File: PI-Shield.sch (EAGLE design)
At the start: 80 parts, among them IC1 PCF8574T, J10 T2I, J11 T2I, J12 T2I, J13 DF13-4P-1.25DSA, J14 DF13-4P-1.25DSA, J15 DF13-4P-1.25DSA, Q1 220mA/50V/3.5Ω, Q2 220mA/50V/3.5Ω, Q3 220mA/50V/3.5Ω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

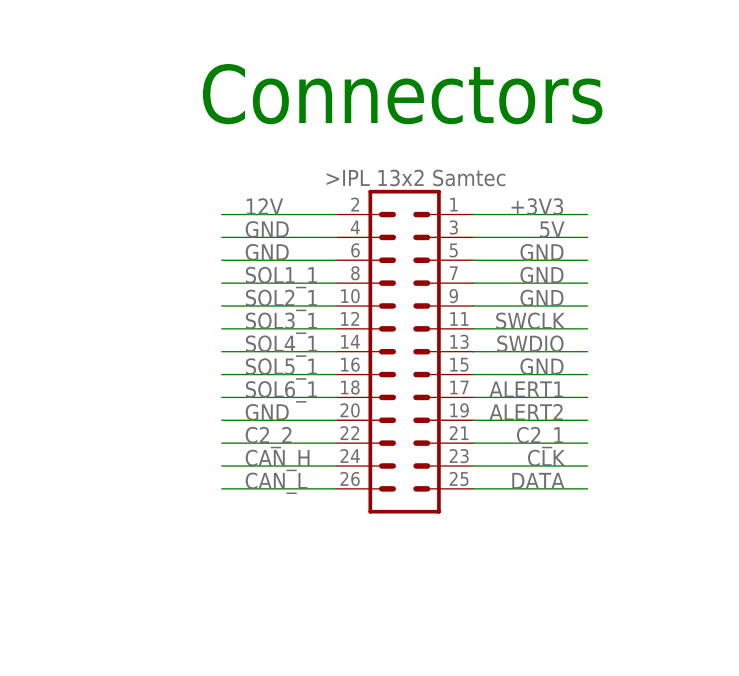
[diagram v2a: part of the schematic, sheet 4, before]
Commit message: Board Update
Changes: [Reduced backplane connector from 26->12 positions, added board outline matching last year's, placement of components]
To Do: [Routing, which should be done within next 24 hrs :P]
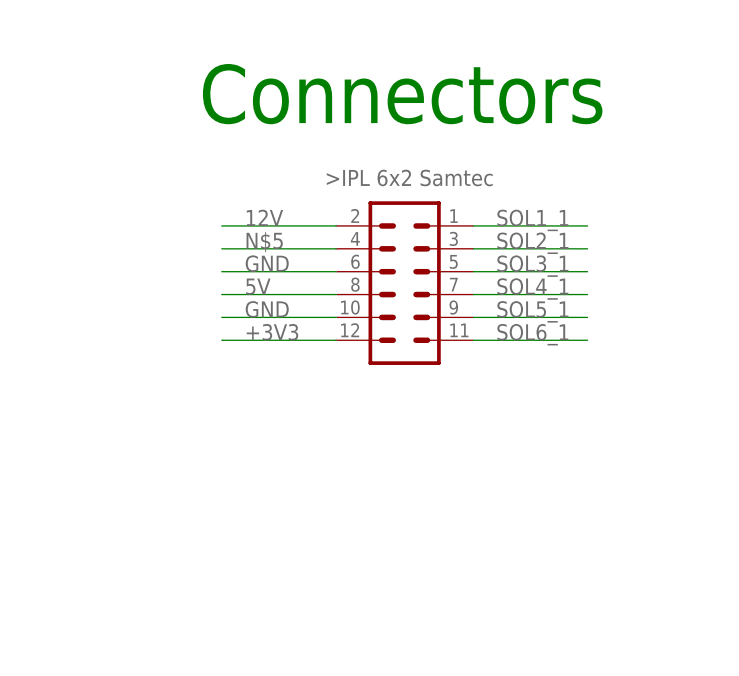
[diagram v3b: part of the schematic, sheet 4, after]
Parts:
- U$3: value IPL_13X2 -> 6X_CONN; device PI-SHIELD, Solenoid-Backplane:IPL_13X2 -> PI-SHIELD, Solenoid-Backplane:6X_CONN
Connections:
- removed net ALERT1: U$3.16
- removed net ALERT2: U$3.18
- removed net C2_1: U$3.20
- removed net C2_2: U$3.19
- removed net DATA: U$3.24
- removed net SWCLK: U$3.10
- removed net SWDIO: U$3.12
- new net N$5: U$3.15
- net +3V3: now also U$3.23; no longer U$3.26
- net 12V: now also U$3.13; no longer U$3.25
- net 5V: now also U$3.19; no longer U$3.2
- net CAN_H: no longer U$3.21
- net CAN_L: no longer U$3.23
- net CLK: no longer U$3.22
- net GND: now also U$3.21; no longer U$3.1, U$3.14, U$3.3, U$3.4, U$3.6, U$3.8
- net SOL1_1: now also U$3.14; no longer U$3.5
- net SOL2_1: now also U$3.16; no longer U$3.7
- net SOL3_1: now also U$3.18; no longer U$3.9
- net SOL4_1: now also U$3.20; no longer U$3.11
- net SOL5_1: now also U$3.22; no longer U$3.13
- net SOL6_1: now also U$3.24; no longer U$3.15
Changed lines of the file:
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@@
 <part name="SUPPLY1" library="supply2" library_urn="urn:adsk.eagle:library:372" deviceset="GND" device=""/>
 <part name="C15" library="SparkFun-Capacitors" library_urn="urn:adsk.eagle:library:510" deviceset="47UF-POLAR" device="-PANASONIC_D-35V-20%" package3d_urn="urn:adsk.eagle:package:37420/1" value="47uF"/>
-<part name="U$3" library="PI-SHIELD, Solenoid-Backplane" deviceset="IPL_13X2" device=""/>
+<part name="U$3" library="PI-SHIELD, Solenoid-Backplane" deviceset="6X_CONN" device=""/>
 </parts>
 <sheets>
@@
 <attribute name="VALUE" x="69.596" y="44.069" size="1.778" layer="96" font="vector"/>
 </instance>
-<instance part="U$3" gate="G$1" x="203.2" y="124.46" smashed="yes"/>
+<instance part="U$3" gate="G$1" x="203.2" y="132.08" smashed="yes"/>
 </instances>
 <busses>
@@
 </segment>
 <segment>
-<pinref part="U$3" gate="G$1" pin="4"/>
-<wire x1="210.82" y1="134.62" x2="223.52" y2="134.62" width="0.1524" layer="91"/>
-<label x="220.98" y="134.62" size="1.778" layer="95" align="bottom-right"/>
-</segment>
-<segment>
-<pinref part="U$3" gate="G$1" pin="6"/>
-<wire x1="210.82" y1="132.08" x2="223.52" y2="132.08" width="0.1524" layer="91"/>
-<label x="220.98" y="132.08" size="1.778" layer="95" align="bottom-right"/>
-</segment>
-<segment>
-<pinref part="U$3" gate="G$1" pin="8"/>
-<wire x1="210.82" y1="129.54" x2="223.52" y2="129.54" width="0.1524" layer="91"/>
-<label x="220.98" y="129.54" size="1.778" layer="95" align="bottom-right"/>
-</segment>
-<segment>
-<pinref part="U$3" gate="G$1" pin="1"/>
-<wire x1="195.58" y1="137.16" x2="182.88" y2="137.16" width="0.1524" layer="91"/>
-<label x="185.42" y="137.16" size="1.778" layer="95"/>
-</segment>
-<segment>
-<pinref part="U$3" gate="G$1" pin="3"/>
-<wire x1="195.58" y1="134.62" x2="182.88" y2="134.62" width="0.1524" layer="91"/>
-<label x="185.42" y="134.62" size="1.778" layer="95"/>
-</segment>
-<segment>
+<wire x1="195.58" y1="133.35" x2="182.88" y2="133.35" width="0.1524" layer="91"/>
+<label x="185.42" y="133.35" size="1.778" layer="95"/>
 <pinref part="U$3" gate="G$1" pin="17"/>
-<wire x1="195.58" y1="116.84" x2="182.88" y2="116.84" width="0.1524" layer="91"/>
-<label x="185.42" y="116.84" size="1.778" layer="95"/>
-</segment>
-<segment>
-<pinref part="U$3" gate="G$1" pin="14"/>
-<wire x1="210.82" y1="121.92" x2="223.52" y2="121.92" width="0.1524" layer="91"/>
-<label x="220.98" y="121.92" size="1.778" layer="95" align="bottom-right"/>
+</segment>
+<segment>
+<wire x1="195.58" y1="128.27" x2="182.88" y2="128.27" width="0.1524" layer="91"/>
+<label x="185.42" y="128.27" size="1.778" layer="95"/>
+<pinref part="U$3" gate="G$1" pin="21"/>
 </segment>
 </net>
@@
 </segment>
 <segment>
-<pinref part="U$3" gate="G$1" pin="25"/>
-<wire x1="195.58" y1="139.7" x2="182.88" y2="139.7" width="0.1524" layer="91"/>
-<label x="185.42" y="139.7" size="1.778" layer="95"/>
+<wire x1="195.58" y1="138.43" x2="182.88" y2="138.43" width="0.1524" layer="91"/>
+<label x="185.42" y="138.43" size="1.778" layer="95"/>
+<pinref part="U$3" gate="G$1" pin="13"/>
 </segment>
 </net>
@@
 </segment>
 <segment>
-<pinref part="U$3" gate="G$1" pin="5"/>
-<wire x1="195.58" y1="132.08" x2="182.88" y2="132.08" width="0.1524" layer="91"/>
-<label x="185.42" y="132.08" size="1.778" layer="95"/>
+<wire x1="223.52" y1="138.43" x2="210.82" y2="138.43" width="0.1524" layer="91"/>
+<label x="213.36" y="138.43" size="1.778" layer="95"/>
+<pinref part="U$3" gate="G$1" pin="14"/>
 </segment>
 </net>
@@
 </segment>
 <segment>
-<pinref part="U$3" gate="G$1" pin="7"/>
-<wire x1="195.58" y1="129.54" x2="182.88" y2="129.54" width="0.1524" layer="91"/>
-<label x="185.42" y="129.54" size="1.778" layer="95"/>
+<wire x1="223.52" y1="135.89" x2="210.82" y2="135.89" width="0.1524" layer="91"/>
+<label x="213.36" y="135.89" size="1.778" layer="95"/>
+<pinref part="U$3" gate="G$1" pin="16"/>
 </segment>
 </net>
@@
 </segment>
 <segment>
-<pinref part="U$3" gate="G$1" pin="9"/>
-<wire x1="195.58" y1="127" x2="182.88" y2="127" width="0.1524" layer="91"/>
-<label x="185.42" y="127" size="1.778" layer="95"/>
+<wire x1="223.52" y1="133.35" x2="210.82" y2="133.35" width="0.1524" layer="91"/>
+<label x="213.36" y="133.35" size="1.778" layer="95"/>
+<pinref part="U$3" gate="G$1" pin="18"/>
 </segment>
 </net>
@@
 </segment>
 <segment>
-<pinref part="U$3" gate="G$1" pin="11"/>
-<wire x1="195.58" y1="124.46" x2="182.88" y2="124.46" width="0.1524" layer="91"/>
-<label x="185.42" y="124.46" size="1.778" layer="95"/>
+<wire x1="223.52" y1="130.81" x2="210.82" y2="130.81" width="0.1524" layer="91"/>
+<label x="213.36" y="130.81" size="1.778" layer="95"/>
+<pinref part="U$3" gate="G$1" pin="20"/>
 </segment>
 </net>
@@
 </segment>
 <segment>
-<pinref part="U$3" gate="G$1" pin="13"/>
-<wire x1="195.58" y1="121.92" x2="182.88" y2="121.92" width="0.1524" layer="91"/>
-<label x="185.42" y="121.92" size="1.778" layer="95"/>
+<wire x1="223.52" y1="128.27" x2="210.82" y2="128.27" width="0.1524" layer="91"/>
+<label x="213.36" y="128.27" size="1.778" layer="95"/>
+<pinref part="U$3" gate="G$1" pin="22"/>
 </segment>
 </net>
@@
 </segment>
 <segment>
-<pinref part="U$3" gate="G$1" pin="15"/>
-<wire x1="195.58" y1="119.38" x2="182.88" y2="119.38" width="0.1524" layer="91"/>
-<label x="185.42" y="119.38" size="1.778" layer="95"/>
+<wire x1="223.52" y1="125.73" x2="210.82" y2="125.73" width="0.1524" layer="91"/>
+<label x="213.36" y="125.73" size="1.778" layer="95"/>
+<pinref part="U$3" gate="G$1" pin="24"/>
 </segment>
 </net>
@@
 </segment>
 <segment>
-<pinref part="U$3" gate="G$1" pin="26"/>
-<wire x1="210.82" y1="139.7" x2="223.52" y2="139.7" width="0.1524" layer="91"/>
-<label x="220.98" y="139.7" size="1.778" layer="95" align="bottom-right"/>
-</segment>
-</net>
-<net name="SWDIO" class="0">
-<segment>
-<pinref part="U$3" gate="G$1" pin="12"/>
-<wire x1="210.82" y1="124.46" x2="223.52" y2="124.46" width="0.1524" layer="91"/>
-<label x="220.98" y="124.46" size="1.778" layer="95" align="bottom-right"/>
-</segment>
-</net>
-<net name="SWCLK" class="0">
-<segment>
-<pinref part="U$3" gate="G$1" pin="10"/>
-<wire x1="210.82" y1="127" x2="223.52" y2="127" width="0.1524" layer="91"/>
-<label x="220.98" y="127" size="1.778" layer="95" align="bottom-right"/>
-</segment>
-</net>
-<net name="C2_1" class="0">
-<segment>
-<pinref part="U$3" gate="G$1" pin="20"/>
-<wire x1="210.82" y1="114.3" x2="223.52" y2="114.3" width="0.1524" layer="91"/>
-<label x="220.98" y="114.3" size="1.778" layer="95" align="bottom-right"/>
-</segment>
-</net>
-<net name="CLK" class="0">
-<segment>
-<pinref part="U$3" gate="G$1" pin="22"/>
-<wire x1="210.82" y1="111.76" x2="223.52" y2="111.76" width="0.1524" layer="91"/>
-<label x="220.98" y="111.76" size="1.778" layer="95" align="bottom-right"/>
-</segment>
-</net>
-<net name="ALERT1" class="0">
-<segment>
-<pinref part="U$3" gate="G$1" pin="16"/>
-<wire x1="210.82" y1="119.38" x2="223.52" y2="119.38" width="0.1524" layer="91"/>
-<label x="220.98" y="119.38" size="1.778" layer="95" align="bottom-right"/>
+<wire x1="182.88" y1="125.73" x2="195.58" y2="125.73" width="0.1524" layer="91"/>
+<pinref part="U$3" gate="G$1" pin="23"/>
+<label x="185.42" y="125.73" size="1.778" layer="95"/>
 </segment>
 </net>
@@
 </segment>
 </net>
+<net name="N$5" class="0">
+<segment>
+<wire x1="195.58" y1="135.89" x2="182.88" y2="135.89" width="0.1524" layer="91"/>
+<label x="185.42" y="135.89" size="1.778" layer="95"/>
+<pinref part="U$3" gate="G$1" pin="15"/>
+</segment>
+</net>
 <net name="5V" class="2">
 <segment>
-<pinref part="U$3" gate="G$1" pin="2"/>
-<wire x1="210.82" y1="137.16" x2="223.52" y2="137.16" width="0.1524" layer="91"/>
-<label x="220.98" y="137.16" size="1.778" layer="95" align="bottom-right"/>
-</segment>
-</net>
-<net name="CAN_H" class="1">
-<segment>
-<pinref part="U$3" gate="G$1" pin="21"/>
-<wire x1="195.58" y1="111.76" x2="182.88" y2="111.76" width="0.1524" layer="91"/>
-<label x="185.42" y="111.76" size="1.778" layer="95"/>
-</segment>
-</net>
-<net name="CAN_L" class="1">
-<segment>
-<pinref part="U$3" gate="G$1" pin="23"/>
-<wire x1="195.58" y1="109.22" x2="182.88" y2="109.22" width="0.1524" layer="91"/>
-<label x="185.42" y="109.22" size="1.778" layer="95"/>
-</segment>
-</net>
-<net name="DATA" class="0">
-<segment>
-<pinref part="U$3" gate="G$1" pin="24"/>
-<wire x1="210.82" y1="109.22" x2="223.52" y2="109.22" width="0.1524" layer="91"/>
-<label x="220.98" y="109.22" size="1.778" layer="95" align="bottom-right"/>
-</segment>
-</net>
-<net name="C2_2" class="0">
-<segment>
+<wire x1="195.58" y1="130.81" x2="182.88" y2="130.81" width="0.1524" layer="91"/>
 <pinref part="U$3" gate="G$1" pin="19"/>
-<wire x1="195.58" y1="114.3" x2="182.88" y2="114.3" width="0.1524" layer="91"/>
-<label x="185.42" y="114.3" size="1.778" layer="95"/>
-</segment>
-</net>
-<net name="ALERT2" class="0">
-<segment>
-<pinref part="U$3" gate="G$1" pin="18"/>
-<wire x1="210.82" y1="116.84" x2="223.52" y2="116.84" width="0.1524" layer="91"/>
-<label x="220.98" y="116.84" size="1.778" layer="95" align="bottom-right"/>
-</segment>
-</net>
+<label x="185.42" y="130.81" size="1.778" layer="95"/>
+</segment>
+</net>

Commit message: Schematic Update
Changes: [FREAKING FORGOT TO LABEL A PIN >:((((]
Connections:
- removed net N$5: U$3.15
- net 12V: now also U$3.15
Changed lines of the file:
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@@
 <pinref part="U$3" gate="G$1" pin="13"/>
+</segment>
+<segment>
+<wire x1="195.58" y1="135.89" x2="182.88" y2="135.89" width="0.1524" layer="91"/>
+<label x="185.42" y="135.89" size="1.778" layer="95"/>
+<pinref part="U$3" gate="G$1" pin="15"/>
 </segment>
 </net>
@@
 </segment>
 </net>
-<net name="N$5" class="0">
-<segment>
-<wire x1="195.58" y1="135.89" x2="182.88" y2="135.89" width="0.1524" layer="91"/>
-<label x="185.42" y="135.89" size="1.778" layer="95"/>
-<pinref part="U$3" gate="G$1" pin="15"/>
-</segment>
-</net>

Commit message: Alumni Design Updates
Changes: [Trace Matched SCL/SDA & TX/RX, added alumni feedback]
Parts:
- removed C11, C12: 4.7uF, SparkFun-Capacitors:22NF/22,000PF-0603-50V-10%
- removed U2: AZ1117EH-3.3TRG1, AZ1117EH-3.3TRG1:AZ1117EH-3.3TRG1
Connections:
- removed net +3V3: IC1.VDD, U$3.23
- net 3V3: now also IC1.VDD, U$3.23; no longer C12.1, U2.OUT
- net 5V: no longer C11.1, U2.IN
- net GND: no longer C11.2, C12.2, U2.ADJ/GND
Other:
- note removed: "Linear Regulator"
- note removed: "Obsolete Product Needs to be replaced"
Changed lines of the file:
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@@
 <part name="R14" library="SparkFun-Resistors" library_urn="urn:adsk.eagle:library:532" deviceset="RESISTOR" device="0603" package3d_urn="urn:adsk.eagle:package:39650/1" value=" "/>
 <part name="R15" library="SparkFun-Resistors" library_urn="urn:adsk.eagle:library:532" deviceset="RESISTOR" device="0603" package3d_urn="urn:adsk.eagle:package:39650/1" value=" "/>
-<part name="U2" library="AZ1117EH-3.3TRG1" deviceset="AZ1117EH-3.3TRG1" device=""/>
-<part name="C11" library="SparkFun-Capacitors" library_urn="urn:adsk.eagle:library:510" deviceset="22NF/22,000PF" device="-0603-50V-10%" package3d_urn="urn:adsk.eagle:package:37414/1" value="4.7uF"/>
-<part name="C12" library="SparkFun-Capacitors" library_urn="urn:adsk.eagle:library:510" deviceset="22NF/22,000PF" device="-0603-50V-10%" package3d_urn="urn:adsk.eagle:package:37414/1" value="4.7uF"/>
 <part name="J2" library="SparkFun-Connectors" deviceset="CONN_04" device=""/>
 <part name="J6" library="SparkFun-Connectors" deviceset="CONN_02" device=""/>
@@
 <part name="R16" library="SparkFun-Resistors" library_urn="urn:adsk.eagle:library:532" deviceset="RESISTOR" device="0603" package3d_urn="urn:adsk.eagle:package:39650/1" value=" "/>
 <part name="GND30" library="supply1" library_urn="urn:adsk.eagle:library:371" deviceset="GND" device=""/>
-<part name="GND32" library="supply1" library_urn="urn:adsk.eagle:library:371" deviceset="GND" device=""/>
 <part name="GND33" library="supply1" library_urn="urn:adsk.eagle:library:371" deviceset="GND" device=""/>
-<part name="GND34" library="supply1" library_urn="urn:adsk.eagle:library:371" deviceset="GND" device=""/>
 <part name="GND35" library="supply1" library_urn="urn:adsk.eagle:library:371" deviceset="GND" device=""/>
 <part name="GND36" library="supply1" library_urn="urn:adsk.eagle:library:371" deviceset="GND" device=""/>
@@
 Note: 2 NMOS for each
 Open Drain Driver (SDA, SCL)</text>
-<text x="40.64" y="160.02" size="1.778" layer="91">Linear Regulator</text>
 <text x="15.24" y="73.66" size="1.778" layer="91">Do NOT solder this 0Ohm resistor
 unless current sensor is not soldered;
@@
 <text x="73.66" y="111.76" size="1.778" layer="91">Need to replace the sensor sensor with one in stock</text>
 <text x="129.54" y="162.56" size="1.778" layer="91">Should replace the ADC with a cheaper one</text>
-<text x="66.04" y="160.02" size="1.778" layer="91">Obsolete Product
-Needs to be replaced</text>
 <text x="7.62" y="43.18" size="1.778" layer="91">Power Indicator LEDs</text>
 <text x="68.58" y="43.18" size="1.778" layer="91">VOC Pin on MCR1101 determines current
@@
 <attribute name="VALUE" x="177.8" y="105.664" size="1.778" layer="96" font="vector" rot="R180" align="top-center"/>
 </instance>
-<instance part="U2" gate="G$1" x="48.26" y="147.32" smashed="yes">
-<attribute name="NAME" x="40.63058125" y="152.40628125" size="1.7802" layer="95"/>
-<attribute name="VALUE" x="40.632559375" y="139.692559375" size="1.779740625" layer="96"/>
-</instance>
-<instance part="C11" gate="G$1" x="30.48" y="142.24" smashed="yes">
-<attribute name="NAME" x="32.004" y="145.161" size="1.778" layer="95" font="vector"/>
-<attribute name="VALUE" x="32.004" y="140.081" size="1.778" layer="96" font="vector"/>
-</instance>
-<instance part="C12" gate="G$1" x="71.12" y="144.78" smashed="yes">
-<attribute name="NAME" x="72.644" y="147.701" size="1.778" layer="95" font="vector"/>
-<attribute name="VALUE" x="72.644" y="142.621" size="1.778" layer="96" font="vector"/>
-</instance>
 <instance part="J2" gate="G$1" x="33.02" y="109.22" smashed="yes">
 <attribute name="VALUE" x="27.94" y="101.854" size="1.778" layer="96" font="vector"/>
@@
 <attribute name="VALUE" x="121.92" y="119.38" size="1.778" layer="96"/>
 </instance>
-<instance part="GND32" gate="1" x="68.58" y="137.16" smashed="yes">
-<attribute name="VALUE" x="66.04" y="134.62" size="1.778" layer="96"/>
-</instance>
 <instance part="GND33" gate="1" x="175.26" y="30.48" smashed="yes">
 <attribute name="VALUE" x="172.72" y="27.94" size="1.778" layer="96"/>
-</instance>
-<instance part="GND34" gate="1" x="30.48" y="134.62" smashed="yes">
-<attribute name="VALUE" x="27.94" y="132.08" size="1.778" layer="96"/>
 </instance>
 <instance part="GND35" gate="1" x="231.14" y="43.18" smashed="yes">
@@
 <wire x1="124.46" y1="127" x2="124.46" y2="124.46" width="0.1524" layer="91"/>
 <pinref part="GND30" gate="1" pin="GND"/>
-</segment>
-<segment>
-<pinref part="C11" gate="G$1" pin="2"/>
-<wire x1="30.48" y1="139.7" x2="30.48" y2="137.16" width="0.1524" layer="91"/>
-<pinref part="GND34" gate="1" pin="GND"/>
-</segment>
-<segment>
-<pinref part="U2" gate="G$1" pin="ADJ/GND"/>
-<wire x1="58.42" y1="144.78" x2="66.04" y2="144.78" width="0.1524" layer="91"/>
-<wire x1="66.04" y1="144.78" x2="66.04" y2="139.7" width="0.1524" layer="91"/>
-<wire x1="66.04" y1="139.7" x2="68.58" y2="139.7" width="0.1524" layer="91"/>
-<pinref part="GND32" gate="1" pin="GND"/>
-<pinref part="C12" gate="G$1" pin="2"/>
-<wire x1="71.12" y1="142.24" x2="71.12" y2="139.7" width="0.1524" layer="91"/>
-<wire x1="71.12" y1="139.7" x2="68.58" y2="139.7" width="0.1524" layer="91"/>
-<junction x="68.58" y="139.7"/>
 </segment>
 <segment>
@@
 <wire x1="233.68" y1="129.54" x2="236.22" y2="129.54" width="0.1524" layer="91"/>
 <label x="236.22" y="129.54" size="1.778" layer="95"/>
-</segment>
-<segment>
-<pinref part="U2" gate="G$1" pin="IN"/>
-<wire x1="38.1" y1="149.86" x2="30.48" y2="149.86" width="0.1524" layer="91"/>
-<pinref part="C11" gate="G$1" pin="1"/>
-<wire x1="30.48" y1="149.86" x2="30.48" y2="147.32" width="0.1524" layer="91"/>
-<wire x1="30.48" y1="149.86" x2="27.94" y2="149.86" width="0.1524" layer="91"/>
-<junction x="30.48" y="149.86"/>
-<wire x1="27.94" y1="149.86" x2="27.94" y2="152.4" width="0.1524" layer="91"/>
-<label x="27.94" y="152.4" size="1.778" layer="95" rot="R180" xref="yes"/>
 </segment>
 <segment>
@@
 <wire x1="213.36" y1="104.14" x2="208.28" y2="104.14" width="0.1524" layer="91"/>
 <label x="208.28" y="104.14" size="1.778" layer="95"/>
-</segment>
-<segment>
-<pinref part="U2" gate="G$1" pin="OUT"/>
-<pinref part="C12" gate="G$1" pin="1"/>
-<wire x1="58.42" y1="149.86" x2="71.12" y2="149.86" width="0.1524" layer="91"/>
-<wire x1="71.12" y1="149.86" x2="71.12" y2="152.4" width="0.1524" layer="91"/>
-<junction x="71.12" y="149.86"/>
-<label x="71.12" y="152.4" size="1.778" layer="95" xref="yes"/>
 </segment>
 <segment>
@@
 </segment>
 </net>
-<net name="+3V3" class="0">
+<net name="SCL" class="0">
+<segment>
+<pinref part="IC1" gate="G$1" pin="SCL"/>
+<wire x1="137.16" y1="68.58" x2="124.46" y2="68.58" width="0.1524" layer="91"/>
+<label x="127" y="68.58" size="1.778" layer="95"/>
+</segment>
+</net>
+<net name="SDA" class="0">
+<segment>
+<pinref part="IC1" gate="G$1" pin="SDA"/>
+<wire x1="137.16" y1="71.12" x2="124.46" y2="71.12" width="0.1524" layer="91"/>
+<label x="127" y="71.12" size="1.778" layer="95"/>
+</segment>
+</net>
+<net name="5V" class="2">
+<segment>
+<wire x1="195.58" y1="130.81" x2="182.88" y2="130.81" width="0.1524" layer="91"/>
+<pinref part="U$3" gate="G$1" pin="19"/>
+<label x="185.42" y="130.81" size="1.778" layer="95"/>
+</segment>
+</net>
+<net name="3V3" class="3">
 <segment>
 <pinref part="IC1" gate="G$1" pin="VDD"/>
@@
 </segment>
 </net>
-<net name="SCL" class="0">
-<segment>
-<pinref part="IC1" gate="G$1" pin="SCL"/>
-<wire x1="137.16" y1="68.58" x2="124.46" y2="68.58" width="0.1524" layer="91"/>
-<label x="127" y="68.58" size="1.778" layer="95"/>
-</segment>
-</net>
-<net name="SDA" class="0">
-<segment>
-<pinref part="IC1" gate="G$1" pin="SDA"/>
-<wire x1="137.16" y1="71.12" x2="124.46" y2="71.12" width="0.1524" layer="91"/>
-<label x="127" y="71.12" size="1.778" layer="95"/>
-</segment>
-</net>
-<net name="5V" class="2">
-<segment>
-<wire x1="195.58" y1="130.81" x2="182.88" y2="130.81" width="0.1524" layer="91"/>
-<pinref part="U$3" gate="G$1" pin="19"/>
-<label x="185.42" y="130.81" size="1.778" layer="95"/>
-</segment>
-</net>
